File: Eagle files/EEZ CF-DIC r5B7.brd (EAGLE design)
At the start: 155 x 90 mm, 280 parts, among them IC1 VIPer35L, IC2 SI8233BB-D-IS1, IC3 LM5041B, IC4 LM258D, IC5 IR11688STRPBF, IC6 LM258D, IC7 TL103W, P1 T910W-50K, Q1 MMBT5551, Q10 BC856C, Q2 C3M0280090D, Q3 C3M0280090D, Q4 NYC0102BLT1G, Q5 IRFP4332PBF, Q6 IRFP4332PBF, Q7 FDD86250-F085, Q8 FDD86250-F085, Q9 BC856C, X1 39-30-3035, X2 22-05-7095, X3 B2B-ZR, X4 39-30-1020

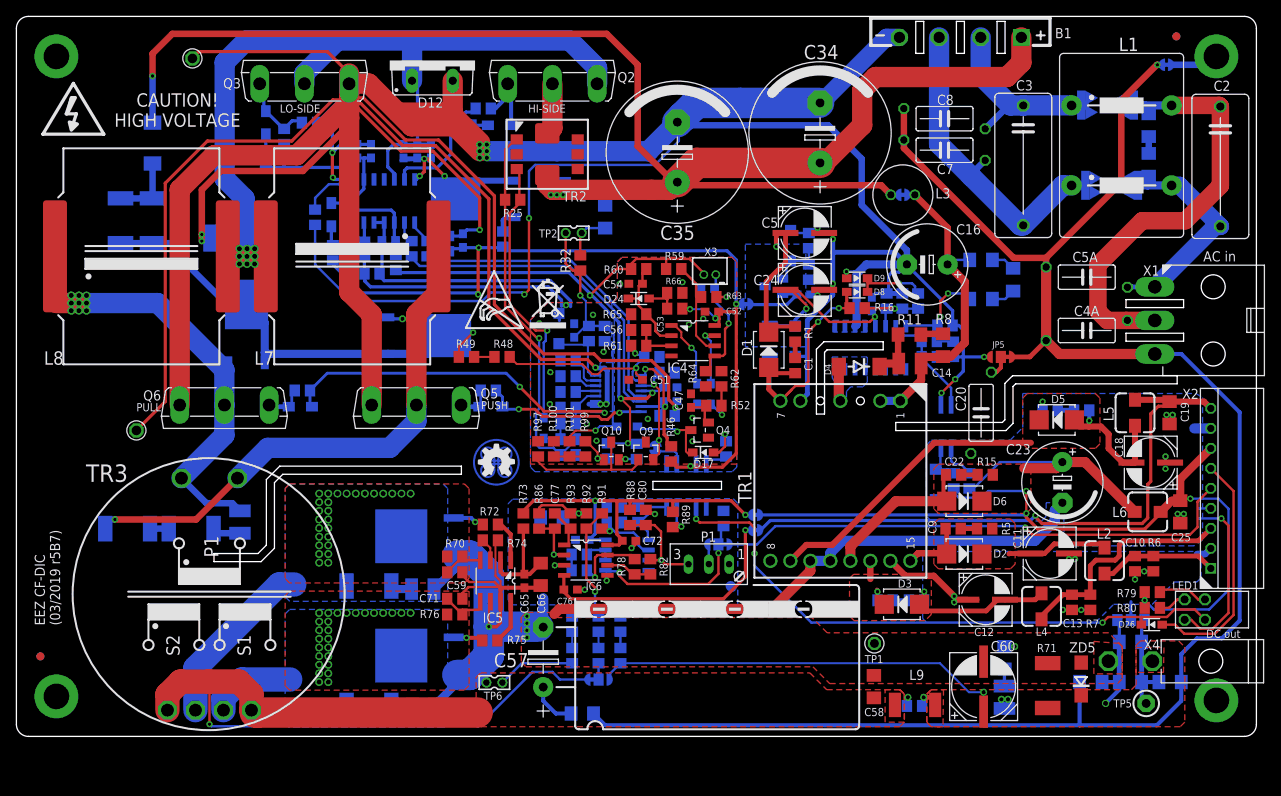
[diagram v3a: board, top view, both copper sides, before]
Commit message: NFB compensation and Viper Rovp adjustment
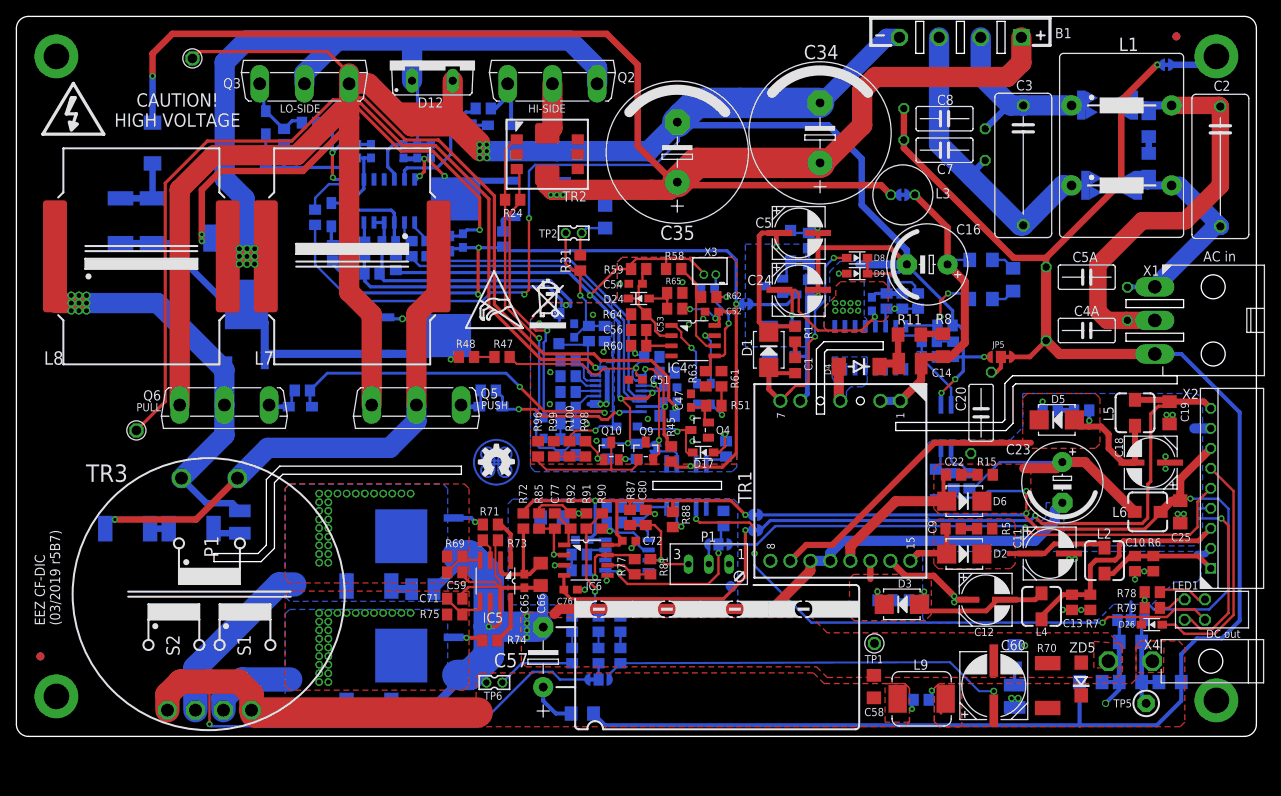
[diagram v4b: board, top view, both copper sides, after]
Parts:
- removed R101: 39K, rcl:R0805
- C14: value 2n2/1kV -> 1n/1kV
- C73: value 1n -> 2n2
- C78: value 470p -> 1n
- D7: value SS100B -> SS110B
- L9: value IHLP2020CZER3R3M11 -> 3u3/5A; device EEZ_inductors_and_transformers:IHLP-2020BZ-11 -> EEZ_inductors_and_transformers:COILCRAFT_HPI0630
- R100: value 18K -> 39K
- R11, R8: value 36K -> 100K
- R16: value N.C. -> 30K
- R17: value 16K -> 1K
- R18: value 1K -> 1K8
- R20: value 1K8 -> 47K
- R21: value 47K -> 1K
- R22: value 1K -> 100K; device rcl:R0805 -> rcl:R1206
- R23: value 100K -> 10R; device rcl:R1206 -> rcl:R0805
- R24: value 10R -> 10K
- R25: value 10K -> 10R
- R26, R37: value 10R -> N.C.
- R27: value N.C. -> 100K; device rcl:R0805 -> rcl:R1206
- R28: value 100K -> 100R; device rcl:R1206 -> rcl:R0805
- R30: value 100R -> 22R/2-3W; device rcl:R0805 -> rcl:R2512
- R31: value 22R/2-3W -> 86K6; device rcl:R2512 -> rcl:R0805
- R32: value 86K6 -> 22R/2-3W; device rcl:R0805 -> rcl:R2512
- R33: value 22R/2-3W -> 30K; device rcl:R2512 -> rcl:R0805
- R34: value 30K -> 1R
- R35: value 1R -> 10R
- R38: value N.C. -> 47K
- R39: value 47K -> 1R
- R40: value 1R -> 22R/2-3W; device rcl:R0805 -> rcl:R2512
- R41: value 22R/2-3W -> 1K; device rcl:R2512 -> rcl:R0805
- R42: value 1K -> N.C.; device rcl:R0805 -> rcl:R2512
- R43, R71: value N.C. -> 10R; device rcl:R2512 -> rcl:R0805
- R44, R54, R75: value 10R -> 1K
- R45: value 1K -> 10R
- R46: value 10R -> 8K2
- R47: value 8K2 -> 86K6
- R49, R74: value 86K6 -> 10R
- R50: value 10R -> 15K
- R51: value 15K -> 4K7
- R52: value 4K7 -> 68K
- R53: value 56K -> 10R
- R55: value 1K -> 6R2
- R56: value 6R2 -> 1K
- R58, R83: value 1K -> 4K7
- R59: value 4K7 -> 5K6
- R60: value 5K6 -> 86K6
- R61: value 86K6 -> 1K
- R62: value 1K -> 30K
- R63: value 30K -> 10K
- R64, R82: value 10K -> 1K
- R66: value 1K -> 120R
- R67: value 120R -> 22R/2-3W; device rcl:R0805 -> rcl:R2512
- R68: value 22R/2-3W -> N.C.; device rcl:R2512 -> rcl:R1210
- R69: value N.C. -> 1K; device rcl:R1210 -> rcl:R0805
- R70: value 1K8 -> N.C.; device rcl:R0805 -> rcl:R2512
- R73: value 10R -> 86K6
- R76: value 1K8 -> 22R/2-3W; device rcl:R0805 -> rcl:R2512
- R77: value 22R/2-3W -> 10K; device rcl:R2512 -> rcl:R0805
- R78: value 10K -> 470R
- R80: value 470R -> 150K
- R81: value 150K -> 10K
- R84: value 30K -> 1K8
- R85: value 1K8 -> 1K
- R86: value 1K -> 27K
- R87: value 86K6 -> 1K8
- R88: value 1K8 -> 3K3
- R89: value 3K3 -> 1K
- R90: value 1K -> 5K6
- R91: value 5K6 -> 7K5
- R92: value 7K5 -> 220R
- R93: value 220R -> N.C.
- R95: value N.C. -> 10K
- R97: value 10K -> 180K
- R98: value 180K -> 39K
- R99: value 39K -> 18K
- moved R68 81.9 mm to (124.8, 5.02), turned to 270 degrees
- moved R41 80.9 mm to (88.7, 35.9)
- moved R42 77.2 mm to (17.0, 64.5)
- moved R70 75.8 mm to (128.9, 6.35), turned to 270 degrees
- moved R71 72.5 mm to (59.2, 26.5), turned to 0 degrees
- moved R69 70.9 mm to (54.8, 22.5), flipped to the top, turned to 180 degrees
- moved R67 69.8 mm to (44.1, 18.8)
- moved R80 66.8 mm to (75.5, 10.1), flipped to the bottom, turned to 270 degrees
- moved R31 65.6 mm to (70.5, 59.2), flipped to the top, turned to 270 degrees
- moved R78 64.8 mm to (142.0, 18.0), turned to 0 degrees
- moved R66 59.5 mm to (113.1, 4.57), flipped to the bottom, turned to 180 degrees
- moved R32 58.9 mm to (21.8, 26.0), flipped to the bottom, turned to 0 degrees
- moved R22 53.4 mm to (78.2, 68.5), turned to 0 degrees
- moved R30 49.8 mm to (13.9, 26.0), turned to 0 degrees
- moved R33 41.1 mm to (43.5, 60.9), turned to 90 degrees
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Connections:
- net +12V: now also R23.2, R36.2, R45.2; no longer R24.2, R37.2, R46.2
- net +2.5VREF: now also R81.2, R87.1; no longer R82.2, R88.1
- net +5VREF: now also R43.1, R58.2, R95.1, R97.1; no longer R44.1, R60.2, R96.1, R98.1
- net +6V_REC: now also R17.1; no longer R18.1
- net 0V: now also R18.2, R38.2, R39.1; no longer R21.2, R40.1, R40.2
- net AGND: now also R33.1, R34.2, R46.2, R50.2, R52.2, R56.2, R61.2, R96.2, R99.2; no longer R100.2, R35.1, R35.2, R47.2, R51.2, R53.2, R58.2, R66.2, R97.2
- net AUX_AC: no longer R16.2
- net CLAMP_C: now also R40.1, R42.1, R48.2; no longer R41.1, R43.1, R49.2
- net CT_OUT+: now also R24.1; no longer R25.1
- net CT_OUT-: now also R24.2, R55.2, R57.1; no longer R25.2, R56.2, R58.1
- net DC_BUS: now also R22.1; no longer R23.1
- net FB: now also R47.1, R56.1, R60.1; no longer R48.1, R57.1, R61.1
- net FB2: now also R21.1; no longer R22.1
- net G1_OUT: now also R71.1; no longer R72.1
- net G2_OUT: now also R74.1; no longer R75.1
- net GATE1: now also R71.2; no longer R72.2
- net GATE2: now also R74.2; no longer R75.2
- net GND: now also R70.1, R73.2; no longer R71.1, R74.2
- net HD: now also R28.2; no longer R29.2
- net HI_OUT: now also R25.2; no longer R27.2
- net LD: now also R29.2; no longer R30.2
- net LO_OUT: now also R35.1, R37.1; no longer R36.1, R38.1
- net L_PUSH: now also R30.2; no longer R31.2
- net N$10: now also R86.1, R90.1; no longer R87.1, R91.1
- net N$100: now also R51.1; no longer R52.1
- net N$11: now also R79.2; no longer R80.2
- net N$12: now also R80.1, R84.2; no longer R81.1, R85.2
- net N$13: now also R49.1; no longer R50.1
- net N$130: now also R41.2; no longer R42.2
- net N$132: now also R77.2, R81.1; no longer R78.2, R82.1
- net N$134: now also R92.2; no longer R93.2
- net N$135: now also R17.2; no longer R18.2
- net N$14: now also R53.1; no longer R54.1
- net N$141: no longer R17.1
- net N$152: now also R20.1; no longer R21.1
- net N$155: now also R16.2; no longer R17.2
- net N$16: now also R78.2; no longer R79.2
- net N$17: now also R32.1; no longer R33.1
- net N$18: now also R73.1; no longer R74.1
- net N$19: now also R52.1; no longer R53.1
- net N$2: now also R27.2, R31.1; no longer R28.2, R32.1
- net N$20: now also R18.1; no longer R20.1
- net N$21: now also R25.1; no longer R26.1
- net N$22: now also R50.1; no longer R51.1
- net N$25: now also R44.1; no longer R45.1
- net N$26: now also R58.1, R62.1; no longer R59.1, R63.1
- net N$28: now also R83.2; no longer R84.2
- net N$29: now also R35.2, R38.1; no longer R36.2, R39.1
- net N$30: now also R47.2, R48.1; no longer R48.2, R49.1
- net N$31: now also R23.1; no longer R24.1
- net N$32: now also R41.1; no longer R42.1
- net N$34: now also R60.2; no longer R61.2
- net N$35: now also R40.2, R42.2; no longer R41.2, R43.2
- net N$36: now also R28.1; no longer R29.1
- net N$37: now also R54.2; no longer R55.2
- net N$40: now also R29.1; no longer R30.1
- net N$42: now also R63.1; no longer R64.1
- net N$45: now also R26.1; no longer R27.1
- net N$46: now also R72.1, R87.2; no longer R73.1, R89.2
- net N$48: now also R33.2; no longer R34.2
- net N$5: now also R30.1, R32.2; no longer R31.1, R33.2
- net N$50: now also R83.1, R90.2, R93.2; no longer R85.1, R92.2, R94.2
- net N$51: now also R51.2, R61.1; no longer R52.2, R62.1
- net N$52: now also R37.2; no longer R38.2
- net N$53: now also R77.1, R82.2; no longer R78.1, R83.2
- net N$54: now also R45.1; no longer R46.1
- net N$56: now also R54.1; no longer R56.1
- net N$59: now also R65.1; no longer R66.1
- net N$6: now also R22.2, R27.1; no longer R23.2, R28.1
- net N$61: now also R96.1; no longer R97.1
- net N$62: now also R95.2; no longer R96.2
- net N$63: now also R36.1; no longer R37.1
- net N$64: now also R82.1, R85.2, R89.1; no longer R83.1, R86.2, R90.1
- net N$66: now also R76.2; no longer R77.2
- net N$67: now also R67.2; no longer R68.2
- net N$68: now also R98.2, R99.1; no longer R101.1, R99.2
- net N$7: now also R59.1, R64.1; no longer R60.1, R65.1
- net N$70: now also R97.2, R98.1; no longer R98.2, R99.1
- net N$73: now also R93.1, R94.2; no longer R94.1, R95.2
- net N$77: now also R94.1; no longer R95.1
- net N$8: now also R68.1; no longer R69.1
- net N$9: now also R86.2; no longer R87.2
- net NFB_OFFSET: now also R85.1, R91.1; no longer R86.1, R93.1
- net OK_A: now also R88.1; no longer R89.1
- net POUT+: now also R66.1; no longer R67.1
- net PREG_OUT+: now also R66.2, R68.2, R70.2, R80.2; no longer R67.2, R69.2, R71.2, R81.2
- net PULL: now also R53.2; no longer R54.2
- net PUSH: now also R49.2; no longer R50.2
- net REF: now also R43.2; no longer R44.2
- net S1_DOT_OUT: now also R75.1; no longer R77.1
- net S2_OUT: now also R67.1, R69.2; no longer R68.1, R70.2
- net SYNC_VCC: now also R72.2; no longer R73.2
- net UVLO: now also R100.2, R31.2, R44.2, R46.1; no longer R101.2, R32.2, R45.2, R47.1
- net U_MON1: now also R89.2; no longer R90.2
- net V+: now also R21.2, R78.1; no longer R22.2, R80.1
- net VD1: now also R69.1; no longer R70.1
- net VD2: now also R75.2; no longer R76.2
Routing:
- net 0V: track 690.8 -> 678.3 mm, vias 23 -> 29
- net N$141: track 9.96 -> 6.28 mm
- net AUX_AC: track 35.2 -> 38.9 mm
- net N$27: track 24.5 -> 26.9 mm
- net CLAMP_C: track 60.4 -> 58.0 mm
- net AUX_REC: track 21.4 -> 22.5 mm
- net PREG_OUT+: track 68.2 -> 69.3 mm
- net POUT+: track 35.1 -> 35.9 mm
- net N$155: track 8.91 -> 9.65 mm
- added copper zone on layer 1, net 0V

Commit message: #7, #8
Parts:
- removed C4A: N.C., EEZ_Lib1:CY075-032X103-ROTATED
- removed C5A: N.C., EEZ_Lib1:CY075-032X103
- removed Q10, Q9: BC856C, transistor:SOT23-BEC
- removed R100, R98: 39K, rcl:R0805
- removed R95, R96: 10K, rcl:R0805
- removed R97: 180K, rcl:R0805
- removed R99: 18K, rcl:R0805
- added F1: 0031.7601, EEZ_Lib1:FUSE_TR5
- added SH4: (no value), EEZ_Lib1:SHORT_NOHOLE
- added U$7: (no value), olimex_logo1:PB_SMALL
- added ZD6: SMAJ58A-TR, EEZ_Lib1:DO214AC
- C4: value N.C. -> CY1Y-4N7; device rcl:C0603 -> EEZ_Lib1:CY075-032X103-ROTATED
- C49: value 2n2 -> 470p
- C5: value EEEFK1V470P -> N.C.; device EEZ_Lib1:CAPAE660X610N -> rcl:C0603
- C50: value 100p -> 470p
- C6: value 1u -> EEEFK1V470P; device rcl:C0805 -> EEZ_Lib1:CAPAE660X610N
- C7: value CY1Y-4N7 -> 1u; device EEZ_Lib1:CY075-032X103 -> rcl:C0805
- R32: value 22R/2-3W -> 10R; device rcl:R2512 -> rcl:R0805
- R33: value 30K -> 22R/2-3W; device rcl:R0805 -> rcl:R2512
- R34: value 1R -> 30K
- R35: value 10R -> 1R
- R37: value N.C. -> 10R
- R38: value 47K -> N.C.
- R39: value 1R -> 47K
- R40: value 22R/2-3W -> 1R; device rcl:R2512 -> rcl:R0805
- R41: value 1K -> 22R/2-3W; device rcl:R0805 -> rcl:R2512
- R42: value N.C. -> 1K; device rcl:R2512 -> rcl:R0805
- R43: value 10R -> N.C.; device rcl:R0805 -> rcl:R2512
- R54: value 1K -> 220p
- R57: value 1K -> 7K5
- ZD4: value BZT52C6V2 -> MMSZ5V1T1G
- ZD5: value SMAJ58A-TR -> BZT52C6V2; device EEZ_Lib1:DO214AC -> EEZ_Lib1:SOD123
- moved R41 80.9 mm to (13.0, 64.5)
- moved ZD5 78.6 mm to (67.8, 51.0), flipped to the bottom
- moved R42 77.2 mm to (88.7, 35.9)
- moved SH3 60.6 mm to (72.5, 46.0), flipped to the top, turned to 90 degrees
- moved R32 42.0 mm to (47.4, 59.2), turned to 90 degrees
- moved R33 41.1 mm to (21.8, 26.0), turned to 0 degrees
- moved C58 40.0 mm to (67.4, 9.72), flipped to the bottom
- moved C4 35.7 mm to (133.8, 50.7), flipped to the top, turned to 0 degrees
- moved R43 30.9 mm to (17.0, 64.5)
- moved C8 26.6 mm to (133.8, 57.4)
- moved R40 24.3 mm to (37.3, 64.9)
- moved U$2 20.9 mm to (74.0, 32.6)
- moved C7 20.4 mm to (99.1, 62.0), flipped to the bottom, turned to 90 degrees
- moved R35 20.4 mm to (44.5, 57.8), turned to 0 degrees
- moved U$4 19.7 mm to (63.2, 32.6)
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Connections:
- removed net N$62: Q10.E, R95.2
- removed net N$68: R100.1, R98.2, R99.1
- removed net N$70: Q10.B, R97.2, R98.1
- new net N$74: OK3.3
- net +12V: now also R37.2; no longer R36.2
- net +5VREF: now also R32.1, ZD4.C; no longer R43.1, R95.1, R97.1
- net 0V: now also C7.2, R40.1, R40.2, SH3.P$1, ZD4.A; no longer C4.2, R38.2, R39.1, SH2.P$1
- net AC_L_IN: now also C8.2; no longer C5A.2
- net AC_N_IN: now also C4.2; no longer C4A.2
- net AGND: now also R35.1, R35.2, SH3.P$2, ZD5.A; no longer OK3.3, Q9.C, R33.1, R34.2, R96.2, R99.2, ZD4.A
- net AUX_REC: now also C6.1; no longer C5.1
- net CLAMP_C: now also R41.1, R43.1; no longer R40.1, R42.1
- net COMP: now also C49.2, R57.1; no longer C50.2, Q9.E
- net CT_OUT-: now also SH2.P$1; no longer R57.1
- net GND: now also ZD6.A; no longer ZD5.A
- net LO_OUT: now also R36.1, R38.1; no longer R35.1, R37.1
- net N$130: now also R42.2; no longer R41.2
- net N$133: now also C7.1; no longer C6.1
- net N$17: now also R33.1; no longer R32.1
- net N$24: now also C5.1; no longer C4.1
- net N$25: now also ZD5.C; no longer ZD4.C
- net N$29: now also R36.2, R39.1; no longer R35.2, R38.1
- net N$32: now also R42.1; no longer R41.1
- net N$35: now also R41.2, R43.2; no longer R40.2, R42.2
- net N$37: now also C50.2; no longer C49.2
- net N$41: no longer C8.2
- net N$43: now also F1.1; no longer B1.AC2, C7.2
- net N$48: now also R34.2; no longer R33.2
- net N$5: now also R33.2; no longer R32.2
- net N$52: now also R38.2; no longer R37.2
- net N$61: now also B1.AC2, F1.2; no longer Q10.C, Q9.B, R96.1
- net N$63: now also R37.1; no longer R36.1
- net PE: now also C4.1; no longer C4A.1, C5A.1, C7.1
- net POUT+: now also SH4.P$2; no longer SH3.P$2
- net PREG_OUT+: now also ZD6.C; no longer ZD5.C
- net REF: now also R32.2; no longer R43.2
- net S_COMM: now also SH4.P$1; no longer SH3.P$1
- net UVLO: no longer R100.2
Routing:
- net 0V: track 678.3 -> 627.6 mm
- net PE: track 224.5 -> 196.4 mm, vias 1 -> 2
- net N$43: track 40.6 -> 22.6 mm
- net PREG_OUT+: track 69.3 -> 80.1 mm
- net +5VREF: track 77.0 -> 68.7 mm
- net N$61: track 17.9 -> 10.6 mm
- net UVLO: track 38.3 -> 31.3 mm, vias 2 -> 1
- net GND: track 201.5 -> 208.3 mm
- net N$70: track 4.95 -> 0.00 mm, vias 1 -> 0
- net N$41: track 24.2 -> 20.1 mm
- net N$68: track 3.94 -> 0.00 mm
- net S_COMM: track 73.1 -> 75.9 mm
- net DC_BUS: track 197.2 -> 194.6 mm
- net N$62: track 2.41 -> 0.00 mm, vias 1 -> 0
- net N$77: track 9.72 -> 11.7 mm
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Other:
- board text added: "EEZ CF-DIC (04/2019 r5B7)"
- board text removed: "EEZ CF-DIC (03/2019 r5B7)"

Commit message: BOM update for #7, #8
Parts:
- R2, R3: value 220K -> 470K
- R54: value 220p -> 220R
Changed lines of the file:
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@@
 <layer number="27" name="tValues" color="14" fill="1" visible="no" active="yes"/>
 <layer number="28" name="bValues" color="10" fill="1" visible="no" active="yes"/>
-<layer number="29" name="tStop" color="7" fill="1" visible="yes" active="yes"/>
-<layer number="30" name="bStop" color="7" fill="1" visible="yes" active="yes"/>
+<layer number="29" name="tStop" color="7" fill="1" visible="no" active="yes"/>
+<layer number="30" name="bStop" color="7" fill="1" visible="no" active="yes"/>
 <layer number="31" name="tCream" color="7" fill="4" visible="no" active="yes"/>
 <layer number="32" name="bCream" color="7" fill="5" visible="no" active="yes"/>
@@
 <attribute name="VALUE" x="122.6185" y="79.756" size="1.016" layer="27" ratio="10" rot="R270"/>
 </element>
-<element name="R3" library="rcl" package="R1206" value="220K" x="141.5435" y="71.4505" smashed="yes" rot="MR270">
+<element name="R3" library="rcl" package="R1206" value="470K" x="141.5435" y="71.4505" smashed="yes" rot="MR270">
 <attribute name="NAME" x="142.877" y="70.5615" size="1.016" layer="26" ratio="10" rot="MR90"/>
 <attribute name="VALUE" x="142.0515" y="73.165" size="1.016" layer="28" ratio="10" rot="MR270"/>
@@
 <attribute name="VALUE" x="145.0959" y="51.5341" size="1.016" layer="27" ratio="10"/>
 </element>
-<element name="R2" library="rcl" package="R1206" value="220K" x="141.5435" y="76.4035" smashed="yes" rot="MR270">
+<element name="R2" library="rcl" package="R1206" value="470K" x="141.5435" y="76.4035" smashed="yes" rot="MR270">
 <attribute name="NAME" x="142.877" y="75.6415" size="1.016" layer="26" ratio="10" rot="MR90"/>
 <attribute name="VALUE" x="142.115" y="78.245" size="1.016" layer="28" ratio="10" rot="MR270"/>
@@
 <attribute name="VALUE" x="57.258" y="84.9825" size="1.27" layer="27" ratio="10" rot="R180"/>
 </element>
-<element name="R54" library="rcl" package="R0805" value="220p" x="68.961" y="39.116" smashed="yes" rot="MR180">
+<element name="R54" library="rcl" package="R0805" value="220R" x="68.961" y="39.116" smashed="yes" rot="MR180">
 <attribute name="NAME" x="70.866" y="39.624" size="1.016" layer="26" ratio="10" rot="MR180"/>
 <attribute name="VALUE" x="67.945" y="39.751" size="1.016" layer="28" ratio="10" rot="MR180"/>
